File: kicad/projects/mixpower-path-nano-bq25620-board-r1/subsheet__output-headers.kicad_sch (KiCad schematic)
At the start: 10 parts, among them J10 HAT, J11 DEBUG, J8 DATA_CONN, J9 DATA_HEADER

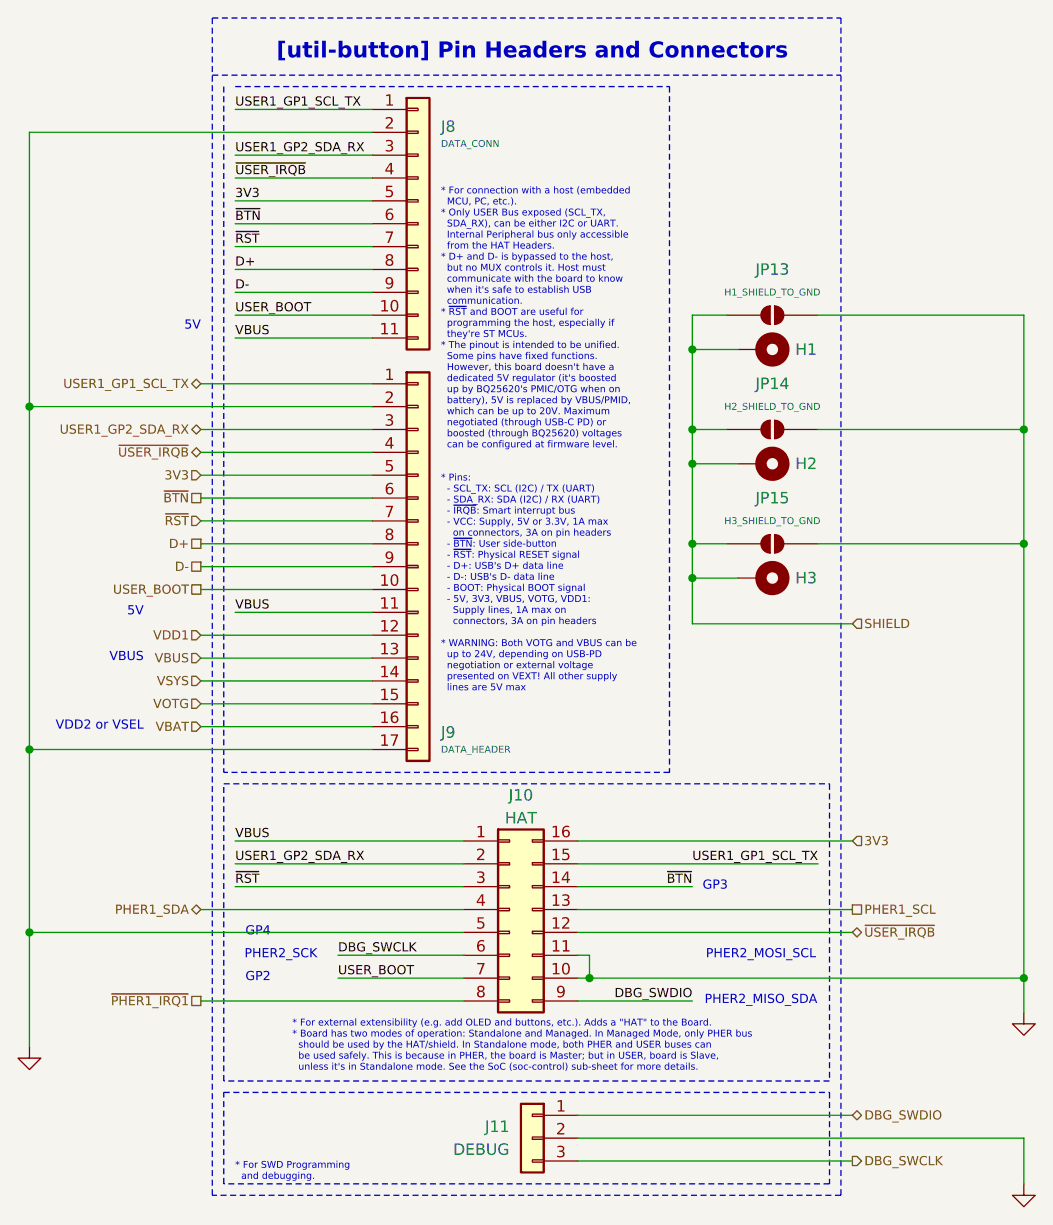
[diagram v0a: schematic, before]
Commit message: fix: put all subsheets in root of the Kicad project, regenerate schematics plots
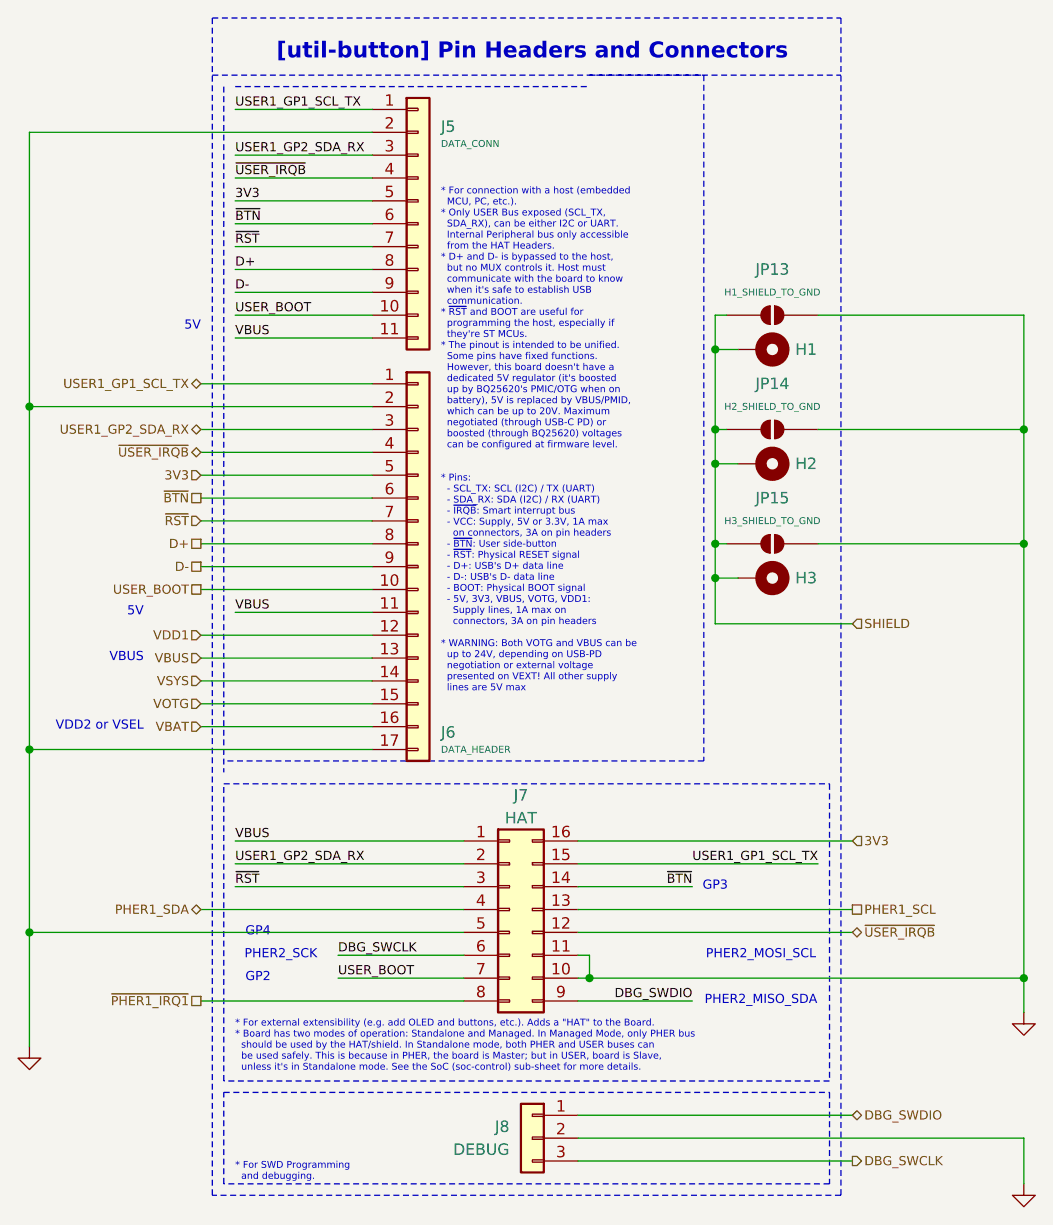
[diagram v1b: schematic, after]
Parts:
- renumbered J8 to J5, J9 to J6, J10 to J7, J11 to J8
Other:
- title: (none) -> mixpower-path-nano-bq25620-board
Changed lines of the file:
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@@
 	(generator_version "10.0")
 	(paper "A4")
+	(title_block
+		(title "mixpower-path-nano-bq25620-board")
+		(date "2026-04-05")
+		(rev "R1")
+	)
 	(rectangle
 		(start 109.22 143.51)
@@
 	(text "* For external extensibility (e.g. add OLED and buttons, etc.). Adds a \"HAT\" to the Board.\n* Board has two modes of operation: Standalone and Managed. In Managed Mode, only PHER bus\n  should be used by the HAT/shield. In Standalone mode, both PHER and USER buses can\n  be used safely. This is because in PHER, the board is Master; but in USER, board is Slave,\n  unless it's in Standalone mode. See the SoC (soc-control) sub-sheet for more details."
 		(exclude_from_sim no)
-		(at 116.84 138.43 0)
+		(at 110.49 138.43 0)
 		(effects
 			(font
@@
 	)
 	(junction
-		(at 161.29 69.85)
-		(diameter 0)
-		(color 0 0 0 0)
-	)
-	(junction
-		(at 161.29 60.96)
+		(at 163.83 73.66)
 		(diameter 0)
 		(color 0 0 0 0)
@@
 	)
 	(junction
-		(at 161.29 86.36)
-		(diameter 0)
-		(color 0 0 0 0)
-	)
-	(junction
 		(at 198.12 82.55)
 		(diameter 0)
@@
 	)
 	(junction
-		(at 161.29 82.55)
+		(at 163.83 60.96)
+		(diameter 0)
+		(color 0 0 0 0)
+	)
+	(junction
+		(at 163.83 82.55)
+		(diameter 0)
+		(color 0 0 0 0)
+	)
+	(junction
+		(at 163.83 86.36)
 		(diameter 0)
 		(color 0 0 0 0)
@@
 	)
 	(junction
-		(at 161.29 73.66)
+		(at 163.83 69.85)
 		(diameter 0)
 		(color 0 0 0 0)
@@
 	(wire
 		(pts
-			(xy 161.29 86.36) (xy 161.29 91.44)
+			(xy 163.83 82.55) (xy 165.1 82.55)
 		)
 		(stroke
@@
 	(wire
 		(pts
-			(xy 161.29 91.44) (xy 179.07 91.44)
+			(xy 163.83 91.44) (xy 179.07 91.44)
 		)
 		(stroke
@@
 		)
 	)
+	(wire
+		(pts
+			(xy 163.83 60.96) (xy 166.37 60.96)
+		)
+		(stroke
+			(width 0)
+			(type default)
+		)
+	)
 	(polyline
 		(pts
-			(xy 158.75 107.95) (xy 109.22 107.95)
+			(xy 162.56 106.68) (xy 109.22 106.68)
 		)
 		(stroke
@@
 	(wire
 		(pts
-			(xy 161.29 82.55) (xy 161.29 86.36)
-		)
-		(stroke
-			(width 0)
-			(type default)
-		)
-	)
-	(wire
-		(pts
 			(xy 148.59 151.13) (xy 179.07 151.13)
 		)
@@
 	(wire
 		(pts
+			(xy 163.83 73.66) (xy 166.37 73.66)
+		)
+		(stroke
+			(width 0)
+			(type default)
+		)
+	)
+	(wire
+		(pts
 			(xy 110.49 120.65) (xy 135.89 120.65)
 		)
@@
 	(wire
 		(pts
+			(xy 163.83 73.66) (xy 163.83 82.55)
+		)
+		(stroke
+			(width 0)
+			(type default)
+		)
+	)
+	(wire
+		(pts
 			(xy 148.59 130.81) (xy 149.86 130.81)
 		)
@@
 	(polyline
 		(pts
-			(xy 149.86 31.75) (xy 158.75 31.75)
+			(xy 149.86 30.48) (xy 162.56 30.48)
 		)
 		(stroke
@@
 		)
 	)
-	(wire
-		(pts
-			(xy 161.29 86.36) (xy 166.37 86.36)
-		)
-		(stroke
-			(width 0)
-			(type default)
-		)
-	)
 	(polyline
 		(pts
@@
 	(wire
 		(pts
+			(xy 163.83 60.96) (xy 163.83 69.85)
+		)
+		(stroke
+			(width 0)
+			(type default)
+		)
+	)
+	(wire
+		(pts
 			(xy 175.26 69.85) (xy 198.12 69.85)
 		)
@@
 	(polyline
 		(pts
-			(xy 158.75 31.75) (xy 158.75 107.95)
+			(xy 162.56 30.48) (xy 162.56 106.68)
 		)
 		(stroke
@@
 	(wire
 		(pts
-			(xy 166.37 60.96) (xy 161.29 60.96)
-		)
-		(stroke
-			(width 0)
-			(type default)
-		)
-	)
-	(wire
-		(pts
 			(xy 110.49 57.15) (xy 125.73 57.15)
 		)
@@
 	(wire
 		(pts
-			(xy 161.29 73.66) (xy 161.29 82.55)
-		)
-		(stroke
-			(width 0)
-			(type default)
-		)
-	)
-	(wire
-		(pts
 			(xy 106.68 95.25) (xy 125.73 95.25)
 		)
@@
 	(wire
 		(pts
-			(xy 161.29 57.15) (xy 161.29 60.96)
-		)
-		(stroke
-			(width 0)
-			(type default)
-		)
-	)
-	(wire
-		(pts
-			(xy 161.29 60.96) (xy 161.29 69.85)
+			(xy 163.83 57.15) (xy 163.83 60.96)
 		)
 		(stroke
@@
 	(wire
 		(pts
-			(xy 161.29 73.66) (xy 166.37 73.66)
+			(xy 163.83 82.55) (xy 163.83 86.36)
 		)
 		(stroke
@@
 	(wire
 		(pts
-			(xy 161.29 57.15) (xy 165.1 57.15)
+			(xy 163.83 57.15) (xy 165.1 57.15)
 		)
 		(stroke
@@
 	(wire
 		(pts
-			(xy 161.29 69.85) (xy 165.1 69.85)
-		)
-		(stroke
-			(width 0)
-			(type default)
-		)
-	)
-	(wire
-		(pts
 			(xy 110.49 52.07) (xy 125.73 52.07)
 		)
@@
 	(wire
 		(pts
-			(xy 161.29 82.55) (xy 165.1 82.55)
-		)
-		(stroke
-			(width 0)
-			(type default)
-		)
-	)
-	(wire
-		(pts
 			(xy 87.63 125.73) (xy 135.89 125.73)
 		)
@@
 	(wire
 		(pts
-			(xy 161.29 69.85) (xy 161.29 73.66)
+			(xy 163.83 69.85) (xy 165.1 69.85)
 		)
 		(stroke
@@
 	(wire
 		(pts
+			(xy 163.83 86.36) (xy 166.37 86.36)
+		)
+		(stroke
+			(width 0)
+			(type default)
+		)
+	)
+	(wire
+		(pts
 			(xy 87.63 105.41) (xy 87.63 125.73)
 		)
@@
 	(wire
 		(pts
+			(xy 163.83 69.85) (xy 163.83 73.66)
+		)
+		(stroke
+			(width 0)
+			(type default)
+		)
+	)
+	(wire
+		(pts
 			(xy 106.68 92.71) (xy 125.73 92.71)
 		)
@@
 		(pts
 			(xy 106.68 64.77) (xy 125.73 64.77)
+		)
+		(stroke
+			(width 0)
+			(type default)
+		)
+	)
+	(wire
+		(pts
+			(xy 163.83 86.36) (xy 163.83 91.44)
 		)
 		(stroke
@@
 		(in_pos_files yes)
 		(dnp no)
-		(property "Reference" "J10"
+		(property "Reference" "J7"
 			(at 142.24 110.49 0)
 			(show_name no)
@@
 			(project "mixpower-path-nano-bq25620-board-r1"
 				(path "/2e43857b-9bf9-460c-948c-ec2cf8a8d6b4/121f6246-4b7d-494d-829b-f1279d4a8ccd"
-					(reference "J10")
+					(reference "J7")
 					(unit 1)
 				)
@@
 		(in_pos_files yes)
 		(dnp no)
-		(property "Reference" "J8"
+		(property "Reference" "J5"
 			(at 133.35 36.1949 0)
 			(show_name no)
@@
 			(project "mixpower-path-nano-bq25620-board-r1"
 				(path "/2e43857b-9bf9-460c-948c-ec2cf8a8d6b4/121f6246-4b7d-494d-829b-f1279d4a8ccd"
-					(reference "J8")
+					(reference "J5")
 					(unit 1)
 				)
@@
 		(in_pos_files yes)
 		(dnp no)
-		(property "Reference" "J9"
+		(property "Reference" "J6"
 			(at 133.35 103.5049 0)
 			(show_name no)
@@
 			(project "mixpower-path-nano-bq25620-board-r1"
 				(path "/2e43857b-9bf9-460c-948c-ec2cf8a8d6b4/121f6246-4b7d-494d-829b-f1279d4a8ccd"
-					(reference "J9")
+					(reference "J6")
 					(unit 1)
 				)
@@
 		(in_pos_files yes)
 		(dnp no)
-		(property "Reference" "#PWR097"
+		(property "Reference" "#PWR070"
 			(at 87.63 144.78 0)
 			(hide yes)
@@
 			(project "mixpower-path-nano-bq25620-board-r1"
 				(path "/2e43857b-9bf9-460c-948c-ec2cf8a8d6b4/121f6246-4b7d-494d-829b-f1279d4a8ccd"
-					(reference "#PWR097")
+					(reference "#PWR070")
 					(unit 1)
 				)
@@
 		(dnp no)
 		(fields_autoplaced yes)
-		(property "Reference" "#PWR098"
+		(property "Reference" "#PWR071"
 			(at 198.12 140.97 0)
 			(hide yes)
@@
 			(project "mixpower-path-nano-bq25620-board-r1"
 				(path "/2e43857b-9bf9-460c-948c-ec2cf8a8d6b4/121f6246-4b7d-494d-829b-f1279d4a8ccd"
-					(reference "#PWR098")
+					(reference "#PWR071")
 					(unit 1)
 				)
@@
 		(dnp no)
 		(fields_autoplaced yes)
-		(property "Reference" "#PWR099"
+		(property "Reference" "#PWR072"
 			(at 198.12 160.02 0)
 			(hide yes)
@@
 			(project "mixpower-path-nano-bq25620-board-r1"
 				(path "/2e43857b-9bf9-460c-948c-ec2cf8a8d6b4/121f6246-4b7d-494d-829b-f1279d4a8ccd"
-					(reference "#PWR099")
+					(reference "#PWR072")
 					(unit 1)
 				)
@@
 		(in_pos_files yes)
 		(dnp no)
-		(property "Reference" "J11"
+		(property "Reference" "J8"
 			(at 140.97 147.3199 0)
 			(show_name no)
@@
 			(project "mixpower-path-nano-bq25620-board-r1"
 				(path "/2e43857b-9bf9-460c-948c-ec2cf8a8d6b4/121f6246-4b7d-494d-829b-f1279d4a8ccd"
-					(reference "J11")
+					(reference "J8")
 					(unit 1)
 				)
